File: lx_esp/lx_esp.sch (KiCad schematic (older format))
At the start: 26 parts, among them J1 Conn_01x02, J2 200LX_02X05, Q1 Dual_Nch_MOSFET, SW1 SW_Push, SW2 SW_SPDT, U1 LTC4365, U2 XC6210, U3 ESP-12F, U4 TRS3238E

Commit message: PCB layout
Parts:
- U2: footprint TO_SOT_Packages_SMD:SOT89-5_Housing_Handsoldering -> TO_SOT_Packages_SMD:SOT-89-5_Housing_Handsoldering
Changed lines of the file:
@@
 	6850 3950 6900 3950
 Wire Wire Line
-	6900 4800 6900 3950
+	6900 3950 6900 4800
 Wire Wire Line
 	5050 3850 5000 3850
@@
 	3000 3850 3000 3750
 Wire Wire Line
-	2600 3750 3000 3750
+	3000 3750 2600 3750
 Connection ~ 2600 3750
 Wire Wire Line
@@
 F 0 "U2" H 3300 3350 60  0000 C CNN
 F 1 "XC6210" H 3300 3450 60  0000 C CNN
-F 2 "TO_SOT_Packages_SMD:SOT89-5_Housing_Handsoldering" H 3300 3400 60  0001 C CNN
+F 2 "TO_SOT_Packages_SMD:SOT-89-5_Housing_Handsoldering" H 3300 3400 60  0001 C CNN
 F 3 "" H 3300 3400 60  0001 C CNN
 	1    3300 3400

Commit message: more pcb layout
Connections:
- net CD: now also U4.17 (DIN5); no longer U4.24 (DIN1)
- net DSR: now also U4.19 (DIN4); no longer U4.22 (DIN3)
- net RI: now also U4.24 (DIN1); no longer U4.17 (DIN5)
- net UART0_RTS: now also U4.23 (DIN2); no longer U4.19 (DIN4)
- net UART0_TXD: now also U4.22 (DIN3); no longer U4.23 (DIN2)
- net at J2.1 (CD): now also U4.12 (DOUT5); no longer U4.5 (DOUT1)
- net at J2.2 (RXD): now also U4.7 (DOUT3); no longer U4.6 (DOUT2)
- net at J2.6 (DSR): now also U4.10 (DOUT4); no longer U4.7 (DOUT3)
- net at J2.8 (CTS): now also U4.6 (DOUT2); no longer U4.10 (DOUT4)
- net at J2.9 (RI): now also U4.5 (DOUT1); no longer U4.12 (DOUT5)
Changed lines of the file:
@@
 	4600 3550 4700 3550
 Wire Wire Line
-	4600 3250 4600 4200
+	4600 3250 4600 3550
+Wire Wire Line
+	4600 3550 4600 4200
 Connection ~ 4600 3550
 Wire Wire Line
-	4100 2200 4100 4250
+	4100 2200 4100 2750
+Wire Wire Line
+	4100 2750 4100 3250
+Wire Wire Line
+	4100 3250 4100 3450
+Wire Wire Line
+	4100 3450 4100 3950
+Wire Wire Line
+	4100 3950 4100 4200
+Wire Wire Line
+	4100 4200 4100 4250
 Wire Wire Line
 	4100 3950 5050 3950
@@
 Connection ~ 4600 4800
 Wire Wire Line
-	4500 3250 5050 3250
+	4500 3250 4600 3250
+Wire Wire Line
+	4600 3250 5050 3250
 Connection ~ 4600 3250
 Wire Wire Line
@@
 Connection ~ 7800 2500
 Wire Wire Line
-	1150 3400 1400 3400
+	1150 3400 1350 3400
+Wire Wire Line
+	1350 3400 1400 3400
 Wire Wire Line
 	1350 3400 1350 3450
@@
 	1350 3750 1350 3800
 Wire Wire Line
-	1150 3950 1150 4050
+	1150 3950 1150 4000
+Wire Wire Line
+	1150 4000 1150 4050
 Connection ~ 1350 3800
 Wire Wire Line
-	1150 2650 1150 3650
+	1150 2650 1150 2900
+Wire Wire Line
+	1150 2900 1150 3400
+Wire Wire Line
+	1150 3400 1150 3650
 Connection ~ 1350 3400
 Wire Wire Line
@@
 Connection ~ 1150 4000
 Wire Wire Line
-	1150 4350 1150 4450
+	1150 4350 1150 4400
+Wire Wire Line
+	1150 4400 1150 4450
 Wire Wire Line
 	1150 4400 1400 4400
@@
 	1700 2950 1700 3000
 Wire Wire Line
-	1700 3000 2200 3000
+	1700 3000 1950 3000
+Wire Wire Line
+	1950 3000 2200 3000
 Wire Wire Line
 	1950 3000 1950 3050
@@
 Connection ~ 4100 3950
 Wire Wire Line
-	4100 4800 4100 4550
+	4100 4800 4100 4600
+Wire Wire Line
+	4100 4600 4100 4550
 Wire Wire Line
 	4100 4200 4350 4200
@@
 Connection ~ 4100 4600
 Wire Wire Line
-	6000 2500 8350 2500
+	6000 2500 7550 2500
+Wire Wire Line
+	7550 2500 7800 2500
+Wire Wire Line
+	7800 2500 8150 2500
+Wire Wire Line
+	8150 2500 8350 2500
 Wire Wire Line
 	3950 3350 3950 4200
@@
 	3800 3250 3800 4250
 Wire Wire Line
-	3750 3250 4200 3250
+	3750 3250 3800 3250
+Wire Wire Line
+	3800 3250 4100 3250
+Wire Wire Line
+	4100 3250 4200 3250
 Wire Wire Line
 	3000 4800 3000 4550
 Connection ~ 3000 4800
 Wire Wire Line
-	3000 4150 3000 4250
+	3000 4150 3000 4200
+Wire Wire Line
+	3000 4200 3000 4250
 Wire Wire Line
 	3950 4200 3000 4200
@@
 Connection ~ 2600 3250
 Wire Wire Line
-	2600 2650 2600 4250
+	2600 2650 2600 3250
+Wire Wire Line
+	2600 3250 2600 3400
+Wire Wire Line
+	2600 3400 2600 3550
+Wire Wire Line
+	2600 3550 2600 3750
+Wire Wire Line
+	2600 3750 2600 4250
 Wire Wire Line
 	900  3000 950  3000
@@
 	950  3000 950  4800
 Wire Wire Line
-	950  4800 10300 4800
+	950  4800 1150 4800
+Wire Wire Line
+	1150 4800 1950 4800
+Wire Wire Line
+	1950 4800 2600 4800
+Wire Wire Line
+	2600 4800 3000 4800
+Wire Wire Line
+	3000 4800 3300 4800
+Wire Wire Line
+	3300 4800 3800 4800
+Wire Wire Line
+	3800 4800 4100 4800
+Wire Wire Line
+	4100 4800 4600 4800
+Wire Wire Line
+	4600 4800 6900 4800
+Wire Wire Line
+	6900 4800 7550 4800
+Wire Wire Line
+	7550 4800 7800 4800
+Wire Wire Line
+	7800 4800 8300 4800
+Wire Wire Line
+	8300 4800 9550 4800
+Wire Wire Line
+	9550 4800 9850 4800
+Wire Wire Line
+	9850 4800 10050 4800
+Wire Wire Line
+	10050 4800 10300 4800
 Wire Wire Line
 	4100 2750 6000 2750
@@
 	9550 2850 9700 2850
 Wire Wire Line
-	9450 3950 10150 3950
-Wire Wire Line
-	9450 3850 10150 3850
-Wire Wire Line
-	9450 3750 9800 3750
-Wire Wire Line
-	9800 3750 9800 3650
-Wire Wire Line
-	9800 3650 10150 3650
-Wire Wire Line
-	9450 3650 9700 3650
-Wire Wire Line
-	9700 3650 9700 3250
-Wire Wire Line
-	9700 3250 10150 3250
-Wire Wire Line
-	9450 3550 9600 3550
-Wire Wire Line
-	9600 3550 9600 3150
-Wire Wire Line
-	9600 3150 10150 3150
-Wire Wire Line
-	9900 3750 10150 3750
+	9950 3750 10150 3750
 Wire Wire Line
 	9450 3250 9500 3250
@@
 	10150 3550 10050 3550
 Wire Wire Line
-	10050 3550 10050 4800
+	10050 3550 10050 4050
+Wire Wire Line
+	10050 4050 10050 4800
 Wire Wire Line
 	10050 4050 10150 4050
@@
 	9450 3350 10150 3350
 Wire Wire Line
-	9900 3750 9900 3050
-Wire Wire Line
-	9900 3050 9450 3050
+	9950 3750 9950 3050
+Wire Wire Line
+	9950 3050 9450 3050
 Wire Wire Line
 	6850 3350 8350 3350
@@
 	6850 3250 8000 3250
 Wire Wire Line
-	8000 3250 8000 3650
-Wire Wire Line
-	8000 3650 8350 3650
-Wire Wire Line
-	6850 3850 8350 3850
+	8000 3250 8000 3750
 Wire Wire Line
 	7900 4600 7900 3050
 Wire Wire Line
 	7900 3050 8350 3050
-Wire Wire Line
-	8000 4650 8000 3750
-Wire Wire Line
-	8000 3750 8350 3750
-Wire Wire Line
-	8100 4700 8100 3950
-Wire Wire Line
-	8100 3950 8350 3950
 Wire Wire Line
 	8350 4300 8300 4300
@@
 Wire Wire Line
 	8100 3250 8350 3250
-Wire Wire Line
-	6850 3550 8350 3550
 NoConn ~ 8350 2850
 NoConn ~ 8350 3150
@@
 Text Label 6900 3650 0    60   ~ 0
 PROG
+Wire Wire Line
+	10150 3150 9600 3150
+Wire Wire Line
+	9600 3150 9600 3950
+Wire Wire Line
+	9600 3950 9450 3950
+Wire Wire Line
+	10150 3250 9800 3250
+Wire Wire Line
+	9800 3250 9800 3750
+Wire Wire Line
+	9800 3750 9450 3750
+Wire Wire Line
+	10150 3650 9850 3650
+Wire Wire Line
+	9850 3650 9850 3850
+Wire Wire Line
+	9850 3850 9450 3850
+Wire Wire Line
+	10150 3850 9900 3850
+Wire Wire Line
+	9900 3850 9900 3550
+Wire Wire Line
+	9900 3550 9750 3550
+Wire Wire Line
+	9750 3550 9750 3650
+Wire Wire Line
+	9750 3650 9450 3650
+Wire Wire Line
+	9450 3550 9700 3550
+Wire Wire Line
+	9700 3550 9700 3950
+Wire Wire Line
+	9700 3950 10150 3950
+Wire Wire Line
+	6850 3550 8100 3550
+Wire Wire Line
+	8100 3550 8100 3950
+Wire Wire Line
+	8100 3950 8350 3950
+Wire Wire Line
+	8000 3750 8350 3750
+Wire Wire Line
+	8350 3850 8000 3850
+Wire Wire Line
+	8000 3850 8000 4650
+Wire Wire Line
+	6850 3850 7450 3850
+Wire Wire Line
+	7450 3850 7450 3650
+Wire Wire Line
+	7450 3650 8350 3650
+Wire Wire Line
+	8350 3550 8200 3550
+Wire Wire Line
+	8200 3550 8200 4700
+Wire Wire Line
+	8200 4700 8100 4700
+Wire Wire Line
+	8100 4700 8100 4700
 $EndSCHEMATC

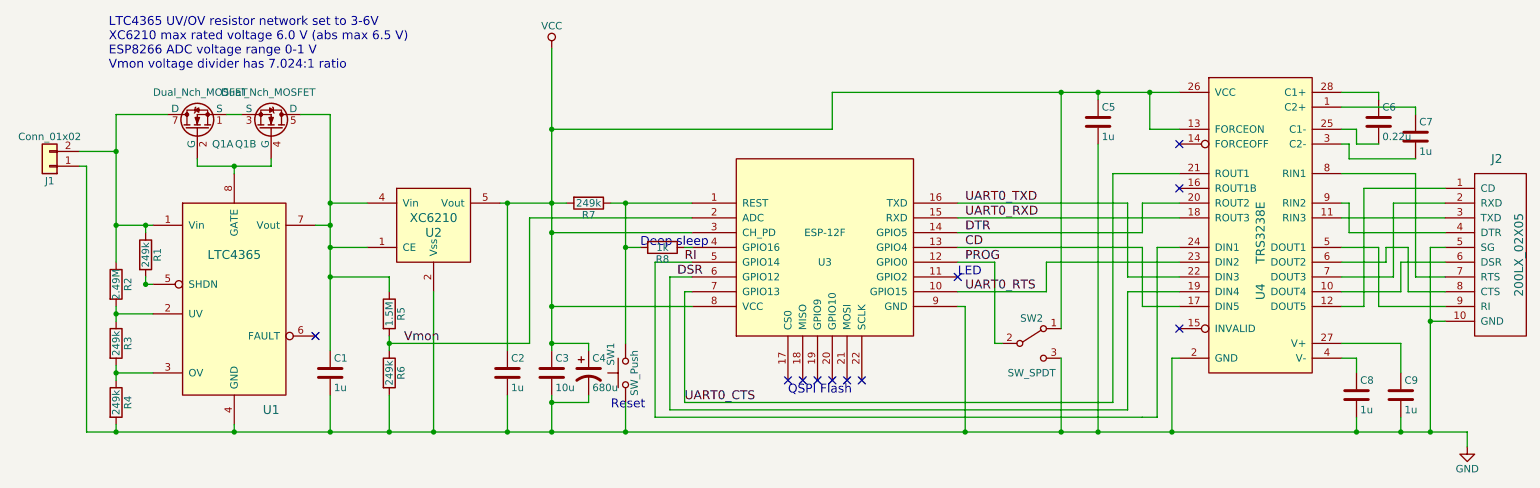
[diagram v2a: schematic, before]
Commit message: narrower pcb for esp
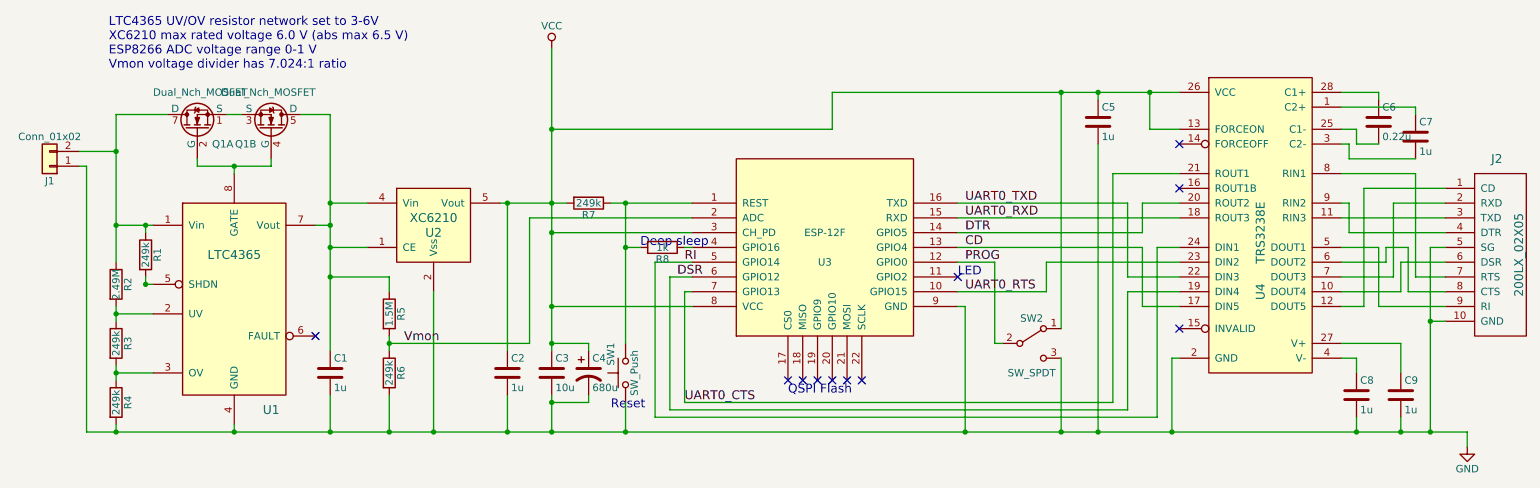
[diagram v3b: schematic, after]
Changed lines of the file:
@@
 	6850 3950 6900 3950
 Wire Wire Line
-	6900 3950 6900 4800
+	6900 4800 6900 3950
 Wire Wire Line
 	5050 3850 5000 3850
@@
 	4800 3650 4800 4700
 Wire Wire Line
-	4800 4700 8100 4700
+	4800 4700 8200 4700
 Connection ~ 7800 4800
 Wire Wire Line
@@
 	4600 3550 4700 3550
 Wire Wire Line
-	4600 3250 4600 3550
-Wire Wire Line
-	4600 3550 4600 4200
+	4600 3250 4600 4200
 Connection ~ 4600 3550
 Wire Wire Line
-	4100 2200 4100 2750
-Wire Wire Line
-	4100 2750 4100 3250
-Wire Wire Line
-	4100 3250 4100 3450
-Wire Wire Line
-	4100 3450 4100 3950
-Wire Wire Line
-	4100 3950 4100 4200
-Wire Wire Line
-	4100 4200 4100 4250
+	4100 2200 4100 4250
 Wire Wire Line
 	4100 3950 5050 3950
@@
 Connection ~ 4600 4800
 Wire Wire Line
-	4500 3250 4600 3250
-Wire Wire Line
-	4600 3250 5050 3250
+	4500 3250 5050 3250
 Connection ~ 4600 3250
 Wire Wire Line
@@
 Connection ~ 7800 2500
 Wire Wire Line
-	1150 3400 1350 3400
-Wire Wire Line
-	1350 3400 1400 3400
+	1150 3400 1400 3400
 Wire Wire Line
 	1350 3400 1350 3450
@@
 	1350 3750 1350 3800
 Wire Wire Line
-	1150 3950 1150 4000
-Wire Wire Line
-	1150 4000 1150 4050
+	1150 3950 1150 4050
 Connection ~ 1350 3800
 Wire Wire Line
-	1150 2650 1150 2900
-Wire Wire Line
-	1150 2900 1150 3400
-Wire Wire Line
-	1150 3400 1150 3650
+	1150 2650 1150 3650
 Connection ~ 1350 3400
 Wire Wire Line
@@
 Connection ~ 1150 4000
 Wire Wire Line
-	1150 4350 1150 4400
-Wire Wire Line
-	1150 4400 1150 4450
+	1150 4350 1150 4450
 Wire Wire Line
 	1150 4400 1400 4400
@@
 	1700 2950 1700 3000
 Wire Wire Line
-	1700 3000 1950 3000
-Wire Wire Line
-	1950 3000 2200 3000
+	1700 3000 2200 3000
 Wire Wire Line
 	1950 3000 1950 3050
@@
 Connection ~ 4100 3950
 Wire Wire Line
-	4100 4800 4100 4600
-Wire Wire Line
-	4100 4600 4100 4550
+	4100 4800 4100 4550
 Wire Wire Line
 	4100 4200 4350 4200
@@
 Connection ~ 4100 4600
 Wire Wire Line
-	6000 2500 7550 2500
-Wire Wire Line
-	7550 2500 7800 2500
-Wire Wire Line
-	7800 2500 8150 2500
-Wire Wire Line
-	8150 2500 8350 2500
+	6000 2500 8350 2500
 Wire Wire Line
 	3950 3350 3950 4200
@@
 	3800 3250 3800 4250
 Wire Wire Line
-	3750 3250 3800 3250
-Wire Wire Line
-	3800 3250 4100 3250
-Wire Wire Line
-	4100 3250 4200 3250
+	3750 3250 4200 3250
 Wire Wire Line
 	3000 4800 3000 4550
 Connection ~ 3000 4800
 Wire Wire Line
-	3000 4150 3000 4200
-Wire Wire Line
-	3000 4200 3000 4250
+	3000 4150 3000 4250
 Wire Wire Line
 	3950 4200 3000 4200
@@
 	3000 3850 3000 3750
 Wire Wire Line
-	3000 3750 2600 3750
+	2600 3750 3000 3750
 Connection ~ 2600 3750
 Wire Wire Line
@@
 Connection ~ 2600 3250
 Wire Wire Line
-	2600 2650 2600 3250
-Wire Wire Line
-	2600 3250 2600 3400
-Wire Wire Line
-	2600 3400 2600 3550
-Wire Wire Line
-	2600 3550 2600 3750
-Wire Wire Line
-	2600 3750 2600 4250
+	2600 2650 2600 4250
 Wire Wire Line
 	900  3000 950  3000
@@
 	950  3000 950  4800
 Wire Wire Line
-	950  4800 1150 4800
-Wire Wire Line
-	1150 4800 1950 4800
-Wire Wire Line
-	1950 4800 2600 4800
-Wire Wire Line
-	2600 4800 3000 4800
-Wire Wire Line
-	3000 4800 3300 4800
-Wire Wire Line
-	3300 4800 3800 4800
-Wire Wire Line
-	3800 4800 4100 4800
-Wire Wire Line
-	4100 4800 4600 4800
-Wire Wire Line
-	4600 4800 6900 4800
-Wire Wire Line
-	6900 4800 7550 4800
-Wire Wire Line
-	7550 4800 7800 4800
-Wire Wire Line
-	7800 4800 8300 4800
-Wire Wire Line
-	8300 4800 9550 4800
-Wire Wire Line
-	9550 4800 9850 4800
-Wire Wire Line
-	9850 4800 10050 4800
-Wire Wire Line
-	10050 4800 10300 4800
+	950  4800 10300 4800
 Wire Wire Line
 	4100 2750 6000 2750
@@
 	10150 3550 10050 3550
 Wire Wire Line
-	10050 3550 10050 4050
-Wire Wire Line
-	10050 4050 10050 4800
+	10050 3550 10050 4800
 Wire Wire Line
 	10050 4050 10150 4050
@@
 	8200 3550 8200 4700
 Wire Wire Line
-	8200 4700 8100 4700
-Wire Wire Line
 	8100 4700 8100 4700
